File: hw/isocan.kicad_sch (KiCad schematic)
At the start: 16 parts, among them U9 TJA1051TK/3,118

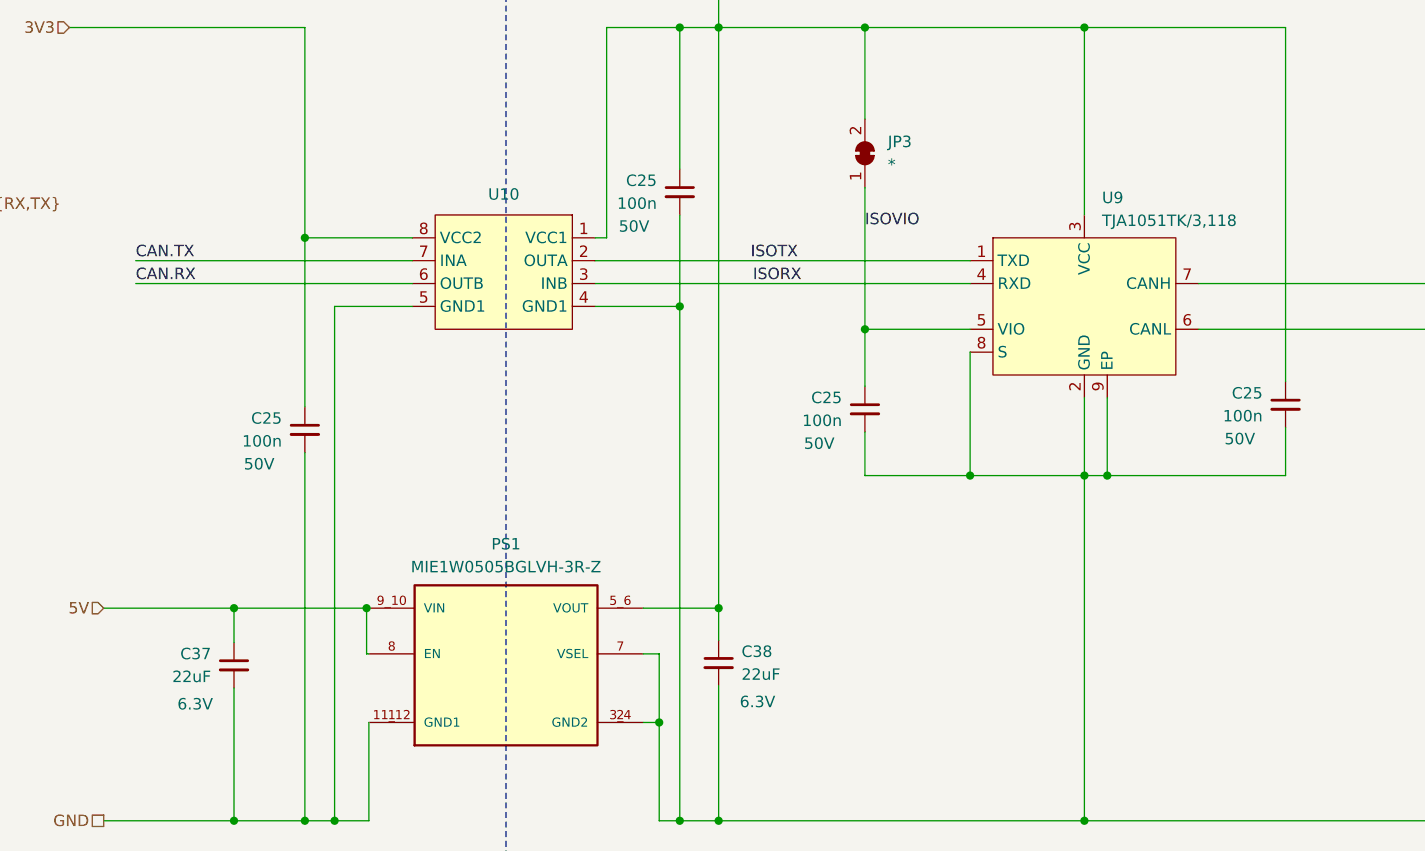
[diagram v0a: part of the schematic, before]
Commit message: [Hw] Optimised components for JLC basic parts
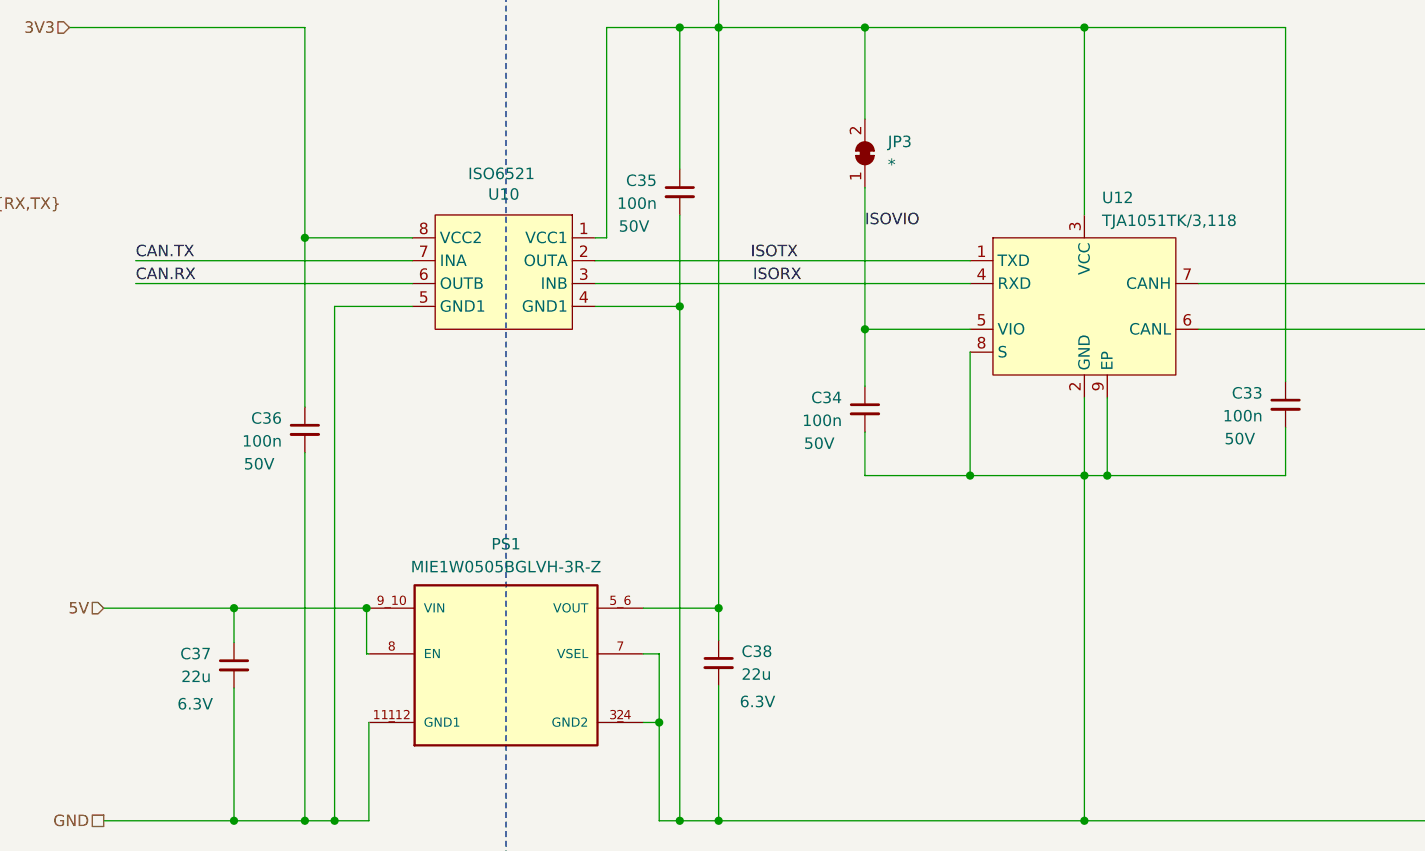
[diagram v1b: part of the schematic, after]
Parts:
- C37, C38: value 22uF -> 22u; footprint Capacitor_SMD:C_0402_1005Metric -> Capacitor_SMD:C_0603_1608Metric; LCSC C415703 -> C59461
- R2: LCSC (none) -> C22787
- U10: value ~ -> ISO6521
- renumbered C25 to C33, C25 to C34, C25 to C35, C25 to C36, U9 to U12

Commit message: [Hw] Version 0.1.0 - sent for manufacture
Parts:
- JP2, JP3, JP4, JP5, JP6, JP7, PS1: now left out of the parts list
- U10: value ISO6521 -> ISO6521F; now left out of the parts list
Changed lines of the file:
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@@
 		(unit 1)
 		(exclude_from_sim no)
-		(in_bom yes)
+		(in_bom no)
 		(on_board yes)
 		(dnp no)
@@
 		(unit 1)
 		(exclude_from_sim no)
-		(in_bom yes)
+		(in_bom no)
 		(on_board yes)
 		(dnp no)
@@
 		(unit 1)
 		(exclude_from_sim no)
-		(in_bom yes)
+		(in_bom no)
 		(on_board yes)
 		(dnp no)
@@
 		(unit 1)
 		(exclude_from_sim no)
-		(in_bom yes)
+		(in_bom no)
 		(on_board yes)
 		(dnp no)
@@
 		(unit 1)
 		(exclude_from_sim no)
-		(in_bom yes)
+		(in_bom no)
 		(on_board yes)
 		(dnp no)
@@
 		(unit 1)
 		(exclude_from_sim no)
-		(in_bom yes)
+		(in_bom no)
 		(on_board yes)
 		(dnp no)
@@
 		(unit 1)
 		(exclude_from_sim no)
-		(in_bom yes)
+		(in_bom no)
 		(on_board yes)
 		(dnp no)
@@
 		(unit 1)
 		(exclude_from_sim no)
-		(in_bom yes)
+		(in_bom no)
 		(on_board yes)
 		(dnp no)
@@
 			)
 		)
-		(property "Value" "ISO6521"
+		(property "Value" "ISO6521F"
 			(at 95.504 62.992 0)
 			(effects

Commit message: [Hw] WIP begun revisions for v0.2.0
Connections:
- net CAN.GND: no longer C33.2, C34.2, C35.2, C38.2, PS1.2 (GND2), PS1.3_4 (GND2), PS1.7 (VSEL), U10.4 (GND1), U12.2 (GND), U12.8 (S), U12.9 (EP)
- new net: C33.2, C34.2, C35.2, C38.2, PS1.2 (GND2), PS1.3_4 (GND2), U10.4 (GND1), U12.2 (GND), U12.8 (S), U12.9 (EP)
- no-connect marks 0 -> 1
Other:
- moved on the sheet: C37, C38, JP6, JP7, PS1, U10

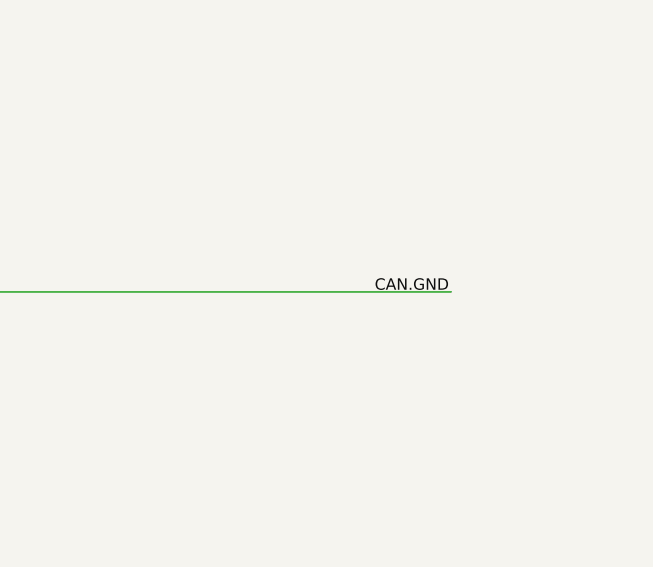
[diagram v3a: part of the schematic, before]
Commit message: [Hw] Unpinched Vcc to 3.4mm width
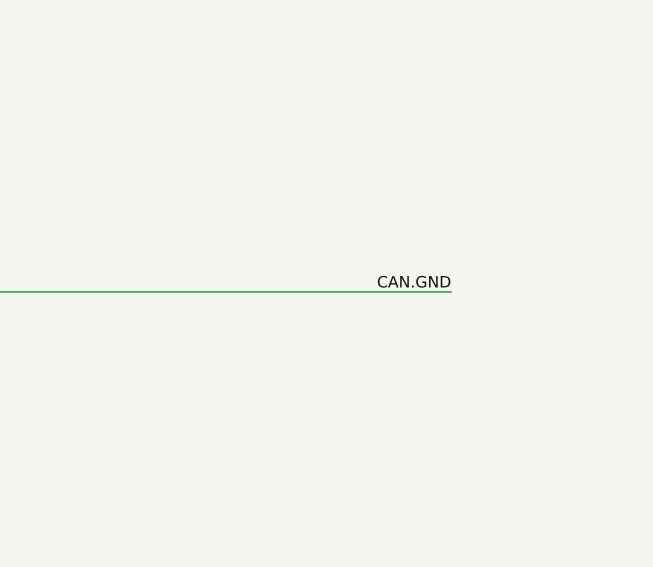
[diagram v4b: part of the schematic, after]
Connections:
- net CAN.GND: now also C33.2, C34.2, C35.2, C38.2, PS1.2 (GND2), PS1.3_4 (GND2), U10.4 (GND1), U12.2 (GND), U12.8 (S), U12.9 (EP)
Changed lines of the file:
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@@
 	)
 	(label "CAN.GND"
-		(at 251.206 134.874 180)
+		(at 251.46 134.62 180)
 		(fields_autoplaced yes)
 		(effects

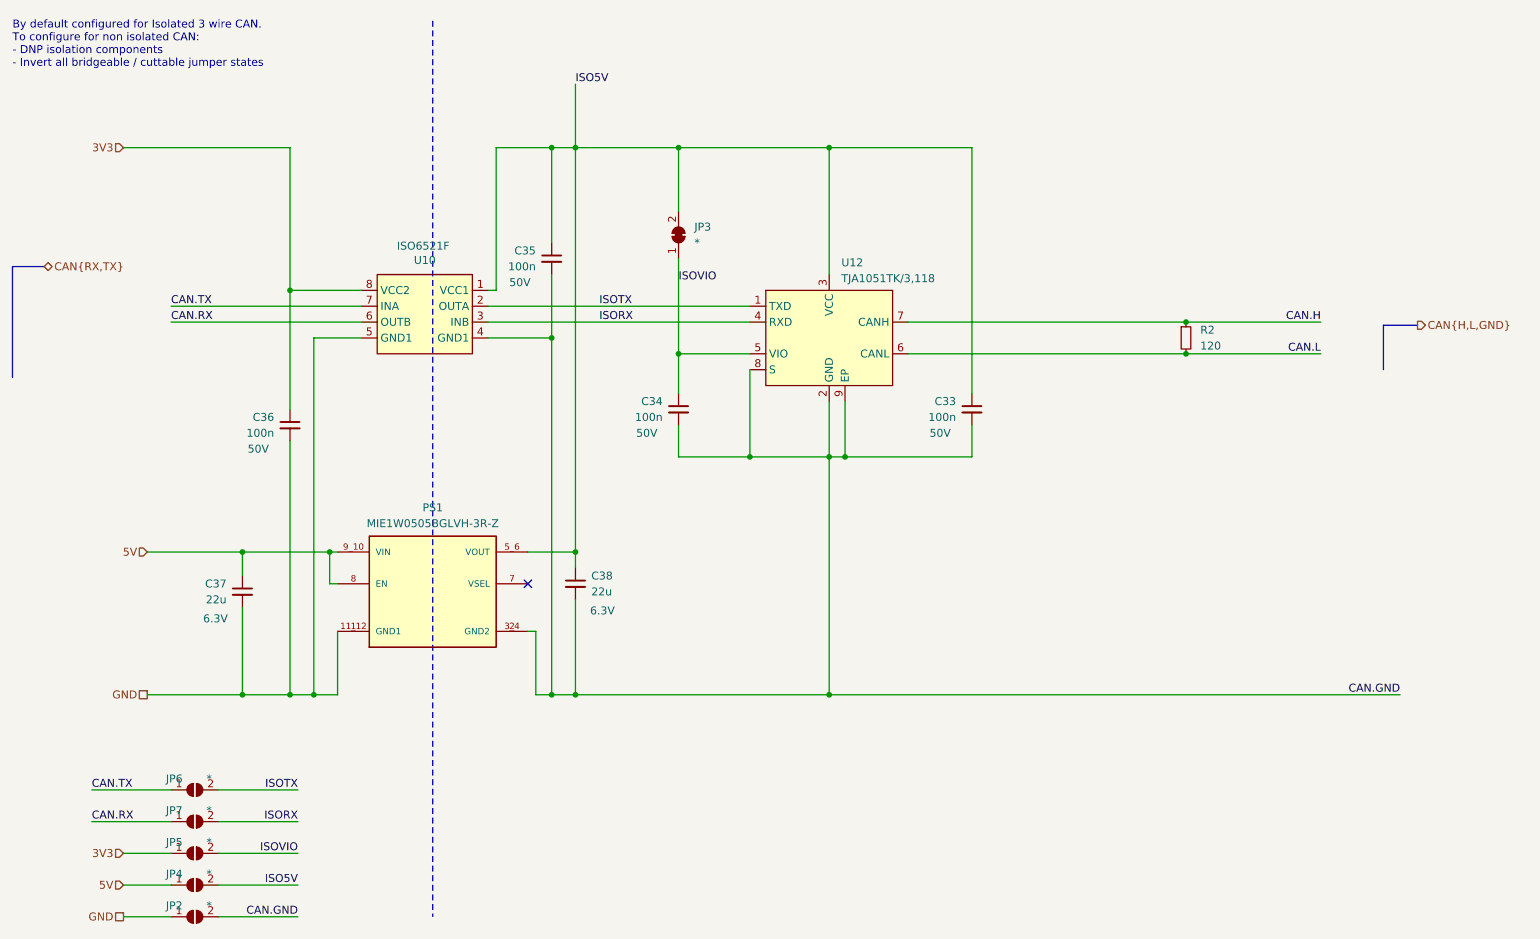
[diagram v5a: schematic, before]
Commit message: [Hw]  LCSC versions of isolated CAN parts
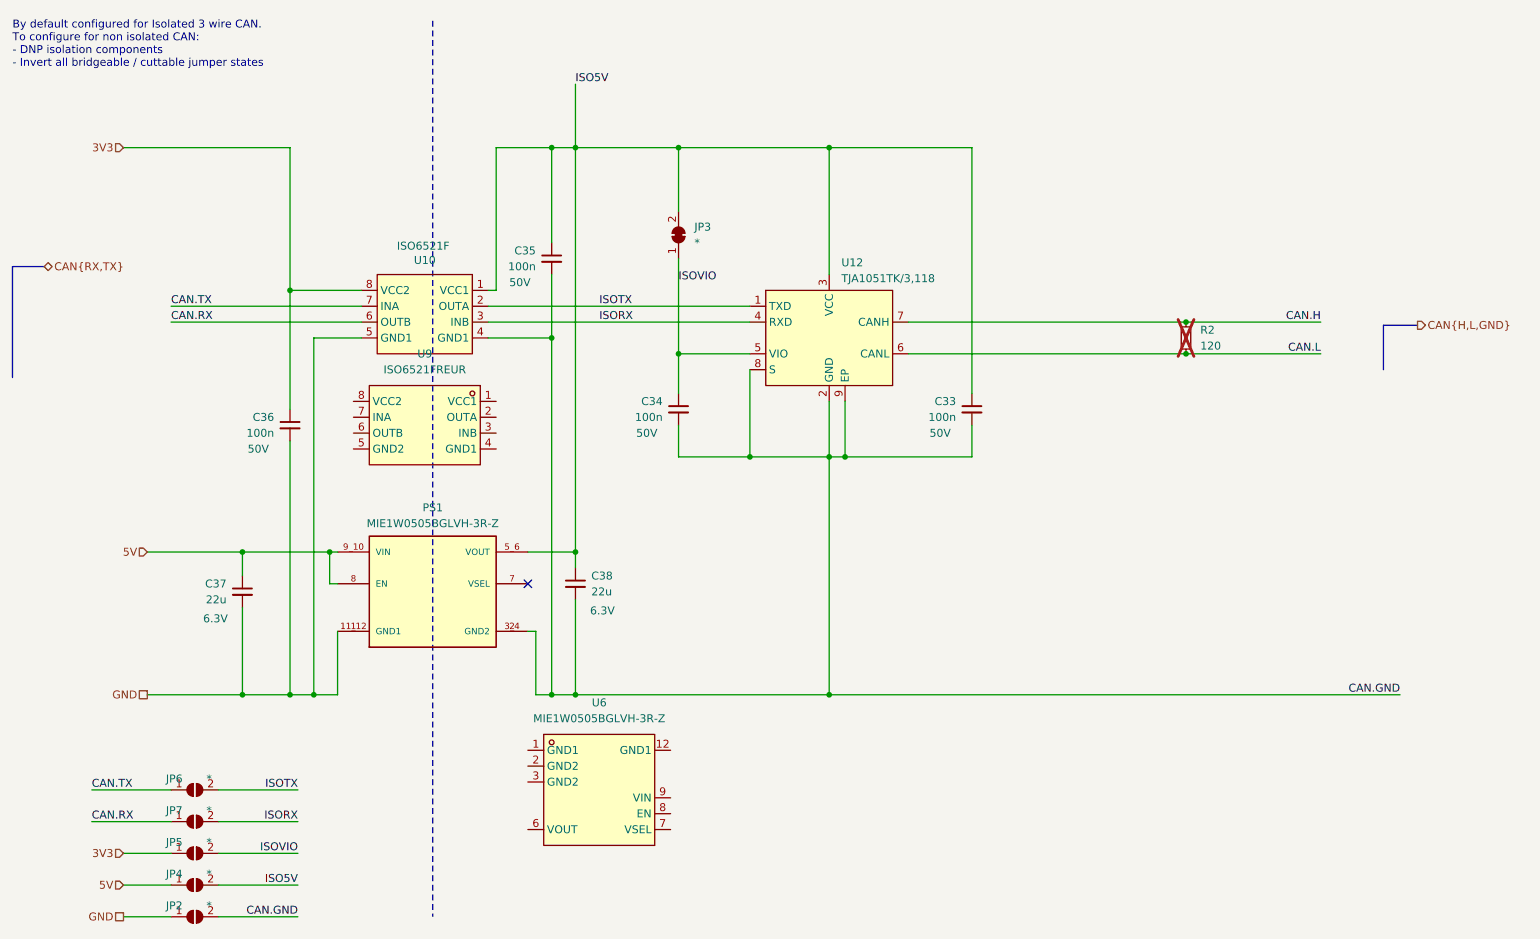
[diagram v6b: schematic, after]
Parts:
- added U6: MIE1W0505BGLVH-3R-Z, easyeda:LGA-12_L4.0-W5.0_MIE1W0505BGLVH, symbol easyeda:MIE1W0505BGLVH-3R-Z
- added U9: ISO6521FREUR, easyeda:XSON-8_L3.0-W2.0-P0.50-BL, symbol easyeda:ISO6521FREUR
- R2: now not fitted
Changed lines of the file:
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@@
 			)
 		)
-		(property "Description" "\nIsolated Module DC DC Converter 1 Output 5V 200mA 3V - 5.5V Input\n"
+		(property "Description" "Isolated Module DC DC Converter 1 Output 5V 200mA 3V - 5.5V Input"
 			(at 96.52 119.38 0)
 			(effects
@@
 				(path "/6a0f293a-1ae1-497a-a3c1-0d8f9e6f81b9/67c38edc-7843-4b4c-b50a-94fd700c0fa2"
 					(reference "PS1")
+					(unit 1)
+				)
+			)
+		)
+	)
+	(symbol
+		(lib_id "easyeda:MIE1W0505BGLVH-3R-Z")
+		(at 123.19 149.86 0)
+		(unit 1)
+		(exclude_from_sim no)
+		(in_bom yes)
+		(on_board yes)
+		(dnp no)
+		(fields_autoplaced yes)
+		(property "Reference" "U6"
+			(at 123.19 135.89 0)
+			(effects
+				(font
+					(size 1.27 1.27)
+				)
+			)
+		)
+		(property "Value" "MIE1W0505BGLVH-3R-Z"
+			(at 123.19 138.43 0)
+			(effects
+				(font
+					(size 1.27 1.27)
+				)
+			)
+		)
+		(property "Footprint" "easyeda:LGA-12_L4.0-W5.0_MIE1W0505BGLVH"
+			(at 123.19 163.83 0)
+			(effects
+				(font
+					(size 1.27 1.27)
+				)
+				(hide yes)
+			)
+		)
+		(property "Datasheet" ""
+			(at 123.19 149.86 0)
+			(effects
+				(font
+					(size 1.27 1.27)
+				)
+				(hide yes)
+			)
+		)
+		(property "Description" ""
+			(at 123.19 149.86 0)
+			(effects
+				(font
+					(size 1.27 1.27)
+				)
+				(hide yes)
+			)
+		)
+		(property "LCSC Part" "C22419841"
+			(at 123.19 166.37 0)
+			(effects
+				(font
+					(size 1.27 1.27)
+				)
+				(hide yes)
+			)
+		)
+		(pin "1"
+		)
+		(pin "6"
+		)
+		(pin "12"
+		)
+		(pin "3"
+		)
+		(pin "7"
+		)
+		(pin "9"
+		)
+		(pin "8"
+		)
+		(pin "2"
+		)
+		(instances
+			(project ""
+				(path "/6a0f293a-1ae1-497a-a3c1-0d8f9e6f81b9/67c38edc-7843-4b4c-b50a-94fd700c0fa2"
+					(reference "U6")
 					(unit 1)
 				)
@@
 				(path "/6a0f293a-1ae1-497a-a3c1-0d8f9e6f81b9/67c38edc-7843-4b4c-b50a-94fd700c0fa2"
 					(reference "JP6")
+					(unit 1)
+				)
+			)
+		)
+	)
+	(symbol
+		(lib_id "easyeda:ISO6521FREUR")
+		(at 95.25 91.44 0)
+		(mirror y)
+		(unit 1)
+		(exclude_from_sim no)
+		(in_bom yes)
+		(on_board yes)
+		(dnp no)
+		(fields_autoplaced yes)
+		(property "Reference" "U9"
+			(at 95.25 80.01 0)
+			(effects
+				(font
+					(size 1.27 1.27)
+				)
+			)
+		)
+		(property "Value" "ISO6521FREUR"
+			(at 95.25 82.55 0)
+			(effects
+				(font
+					(size 1.27 1.27)
+				)
+			)
+		)
+		(property "Footprint" "easyeda:XSON-8_L3.0-W2.0-P0.50-BL"
+			(at 95.25 102.87 0)
+			(effects
+				(font
+					(size 1.27 1.27)
+				)
+				(hide yes)
+			)
+		)
+		(property "Datasheet" ""
+			(at 95.25 91.44 0)
+			(effects
+				(font
+					(size 1.27 1.27)
+				)
+				(hide yes)
+			)
+		)
+		(property "Description" ""
+			(at 95.25 91.44 0)
+			(effects
+				(font
+					(size 1.27 1.27)
+				)
+				(hide yes)
+			)
+		)
+		(property "LCSC Part" "C22399233"
+			(at 95.25 105.41 0)
+			(effects
+				(font
+					(size 1.27 1.27)
+				)
+				(hide yes)
+			)
+		)
+		(pin "7"
+		)
+		(pin "6"
+		)
+		(pin "5"
+		)
+		(pin "3"
+		)
+		(pin "4"
+		)
+		(pin "8"
+		)
+		(pin "1"
+		)
+		(pin "2"
+		)
+		(instances
+			(project ""
+				(path "/6a0f293a-1ae1-497a-a3c1-0d8f9e6f81b9/67c38edc-7843-4b4c-b50a-94fd700c0fa2"
+					(reference "U9")
 					(unit 1)
 				)
@@
 		(in_bom yes)
 		(on_board yes)
-		(dnp no)
+		(dnp yes)
 		(fields_autoplaced yes)
 		(property "Reference" "R2"
